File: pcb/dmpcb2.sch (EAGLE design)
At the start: 74 parts, among them IC1 7805DT, IC2 L293D, IC4 LM358D, IC5 LM358D, J7 SJ-3523-SMT-TR, Q1 IRF530, Q2 IRF530

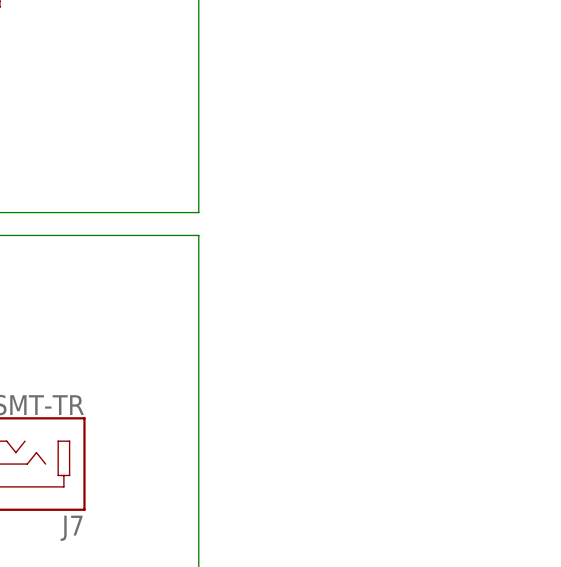
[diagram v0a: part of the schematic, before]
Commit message: added second jack for midi, not too sure if position is good. thinking about putting pads on the bottom of the board and making the jack optional?
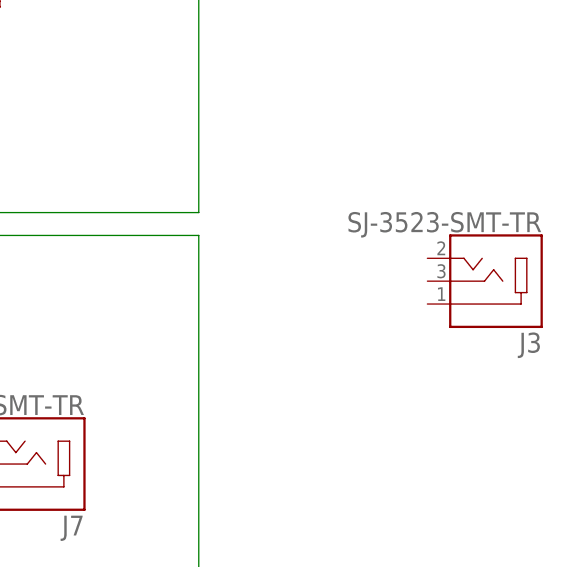
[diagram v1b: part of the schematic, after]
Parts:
- added J3: SJ-3523-SMT-TR, SJ-3523-SMT-TR:SJ-3523-SMT-TR
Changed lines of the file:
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@@
 <part name="GND30" library="supply1" library_urn="urn:adsk.eagle:library:371" deviceset="GND" device=""/>
 <part name="SUPPLY18" library="supply2" library_urn="urn:adsk.eagle:library:372" deviceset="+5V" device=""/>
+<part name="J3" library="SJ-3523-SMT-TR" deviceset="SJ-3523-SMT-TR" device=""/>
 </parts>
 <sheets>
@@
 <attribute name="VALUE" x="376.555" y="9.525" size="1.778" layer="96" rot="R270"/>
 </instance>
+<instance part="J3" gate="G$1" x="434.34" y="-10.16" smashed="yes" rot="R180">
+<attribute name="NAME" x="439.440409375" y="-15.897959375" size="2.201440625" layer="95" rot="R180"/>
+<attribute name="VALUE" x="439.44061875" y="-2.50906875" size="2.20203125" layer="96" rot="R180"/>
+</instance>
 </instances>

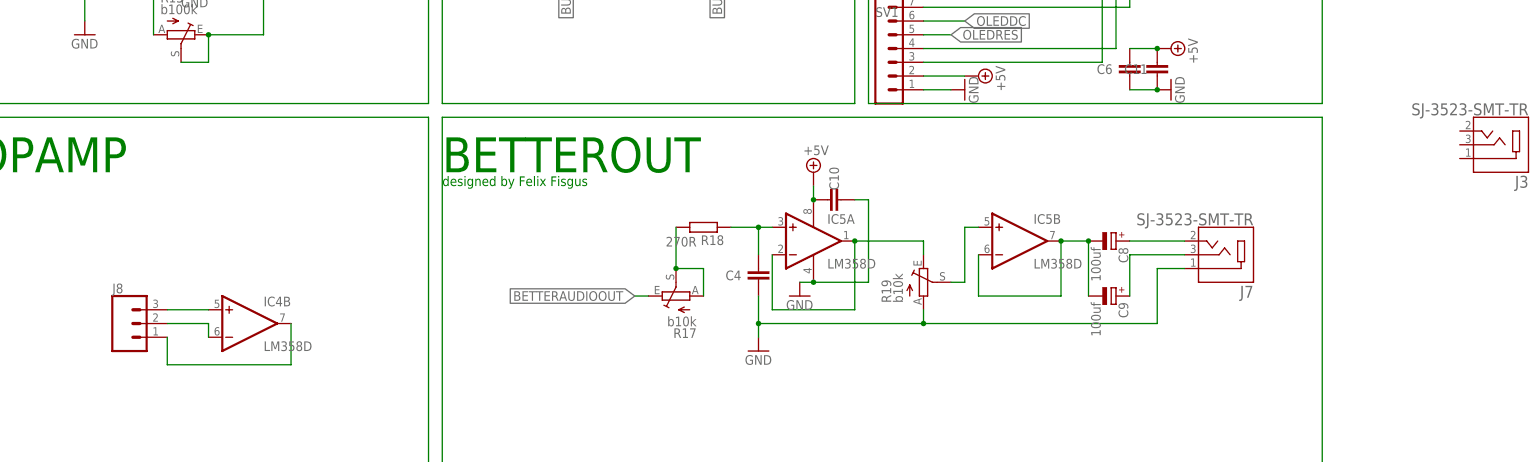
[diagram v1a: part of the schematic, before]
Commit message: removed second 3.5mm jack, drc comes back clean
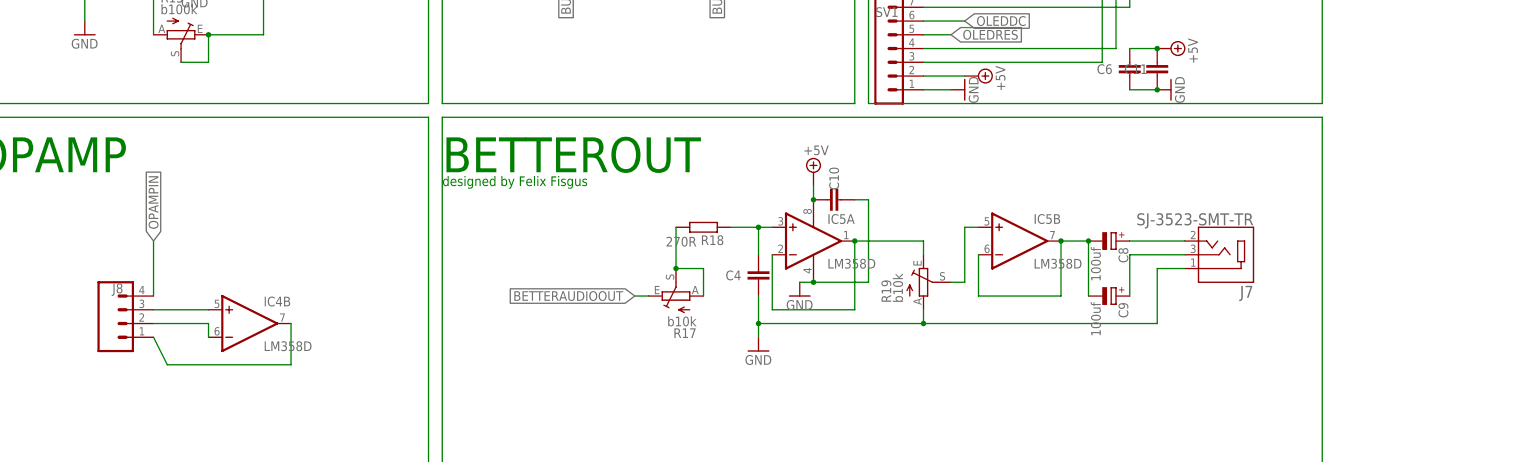
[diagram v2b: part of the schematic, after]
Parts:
- removed J3: SJ-3523-SMT-TR, SJ-3523-SMT-TR:SJ-3523-SMT-TR
- J8: device SparkFun-Connectors:CONN_03LOCK_LONGPADS -> SparkFun-Connectors:CONN_04
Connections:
- net OPAMPIN: now also J8.4
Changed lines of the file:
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@@
 <part name="GND14" library="supply1" library_urn="urn:adsk.eagle:library:371" deviceset="GND" device=""/>
 <part name="SUPPLY15" library="supply2" library_urn="urn:adsk.eagle:library:372" deviceset="+5V" device=""/>
-<part name="J8" library="SparkFun-Connectors" library_urn="urn:adsk.eagle:library:513" deviceset="CONN_03" device="LOCK_LONGPADS" package3d_urn="urn:adsk.eagle:package:38065/1"/>
+<part name="J8" library="SparkFun-Connectors" library_urn="urn:adsk.eagle:library:513" deviceset="CONN_04" device="" package3d_urn="urn:adsk.eagle:package:38085/1"/>
 <part name="X1" library="con-wago-500" library_urn="urn:adsk.eagle:library:195" deviceset="W237-102" device="" package3d_urn="urn:adsk.eagle:package:10688/1"/>
 <part name="SOCKET_IN" library="con-lstb" library_urn="urn:adsk.eagle:library:162" deviceset="MA05-1" device="" package3d_urn="urn:adsk.eagle:package:8332/1"/>
@@
 <part name="GND30" library="supply1" library_urn="urn:adsk.eagle:library:371" deviceset="GND" device=""/>
 <part name="SUPPLY18" library="supply2" library_urn="urn:adsk.eagle:library:372" deviceset="+5V" device=""/>
-<part name="J3" library="SJ-3523-SMT-TR" deviceset="SJ-3523-SMT-TR" device=""/>
 </parts>
 <sheets>
@@
 <attribute name="VALUE" x="222.885" y="85.725" size="1.778" layer="96" rot="R180"/>
 </instance>
-<instance part="J8" gate="J$1" x="180.34" y="-43.18" smashed="yes">
+<instance part="J8" gate="G$1" x="180.34" y="-43.18" smashed="yes">
 <attribute name="VALUE" x="177.8" y="-50.546" size="1.778" layer="96" font="vector"/>
 <attribute name="NAME" x="177.8" y="-37.592" size="1.778" layer="95" font="vector"/>
@@
 <instance part="SUPPLY18" gate="+5V" x="373.38" y="7.62" smashed="yes" rot="R270">
 <attribute name="VALUE" x="376.555" y="9.525" size="1.778" layer="96" rot="R270"/>
-</instance>
-<instance part="J3" gate="G$1" x="434.34" y="-10.16" smashed="yes" rot="R180">
-<attribute name="NAME" x="439.440409375" y="-15.897959375" size="2.201440625" layer="95" rot="R180"/>
-<attribute name="VALUE" x="439.44061875" y="-2.50906875" size="2.20203125" layer="96" rot="R180"/>
 </instance>
 </instances>
@@
 <label x="182.88" y="33.02" size="1.778" layer="95" rot="R180" xref="yes"/>
 </segment>
+<segment>
+<pinref part="J8" gate="G$1" pin="4"/>
+<wire x1="185.42" y1="-38.1" x2="185.42" y2="-27.94" width="0.1524" layer="91"/>
+<label x="185.42" y="-27.94" size="1.778" layer="95" rot="R90" xref="yes"/>
+</segment>
 </net>
 <net name="OPAMPOUT" class="0">
@@
 <segment>
 <pinref part="IC4" gate="B" pin="+IN"/>
-<pinref part="J8" gate="J$1" pin="3"/>
-<wire x1="195.58" y1="-40.64" x2="187.96" y2="-40.64" width="0.1524" layer="91"/>
+<pinref part="J8" gate="G$1" pin="3"/>
+<wire x1="195.58" y1="-40.64" x2="185.42" y2="-40.64" width="0.1524" layer="91"/>
 </segment>
 </net>
@@
 <segment>
 <pinref part="IC4" gate="B" pin="-IN"/>
-<pinref part="J8" gate="J$1" pin="2"/>
+<pinref part="J8" gate="G$1" pin="2"/>
 <wire x1="195.58" y1="-45.72" x2="195.58" y2="-43.18" width="0.1524" layer="91"/>
-<wire x1="195.58" y1="-43.18" x2="187.96" y2="-43.18" width="0.1524" layer="91"/>
+<wire x1="195.58" y1="-43.18" x2="185.42" y2="-43.18" width="0.1524" layer="91"/>
 </segment>
 </net>
 <net name="N$75" class="0">
 <segment>
-<pinref part="J8" gate="J$1" pin="1"/>
-<wire x1="187.96" y1="-45.72" x2="187.96" y2="-50.8" width="0.1524" layer="91"/>
+<pinref part="J8" gate="G$1" pin="1"/>
+<wire x1="185.42" y1="-45.72" x2="187.96" y2="-50.8" width="0.1524" layer="91"/>
 <wire x1="187.96" y1="-50.8" x2="210.82" y2="-50.8" width="0.1524" layer="91"/>
 <pinref part="IC4" gate="B" pin="OUT"/>

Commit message: screws fit
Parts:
- added SOCKET_IN1: (no value), con-lstb:MA05-1
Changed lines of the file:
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@@
 <part name="GND30" library="supply1" library_urn="urn:adsk.eagle:library:371" deviceset="GND" device=""/>
 <part name="SUPPLY18" library="supply2" library_urn="urn:adsk.eagle:library:372" deviceset="+5V" device=""/>
+<part name="SOCKET_IN1" library="con-lstb" library_urn="urn:adsk.eagle:library:162" deviceset="MA05-1" device="" package3d_urn="urn:adsk.eagle:package:8332/1"/>
 </parts>
 <sheets>
@@
 <attribute name="VALUE" x="376.555" y="9.525" size="1.778" layer="96" rot="R270"/>
 </instance>
+<instance part="SOCKET_IN1" gate="G$1" x="350.52" y="25.4" smashed="yes" rot="R270">
+<attribute name="VALUE" x="340.614" y="27.94" size="1.778" layer="96" font="vector" rot="R270"/>
+<attribute name="NAME" x="358.648" y="27.94" size="1.778" layer="95" font="vector" rot="R270"/>
+</instance>
 </instances>
